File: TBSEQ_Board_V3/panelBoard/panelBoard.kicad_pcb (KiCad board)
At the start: 2 copper layers, 200 x 130.3 mm, 90 parts, among them J1 Conn_01x05, J14 Conn_01x05, U7 HT16K33_28SOP-A_

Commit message: V3Board
panelBoardアートワーク完了 ラベル未記入
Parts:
- removed J14: Conn_01x05, Connector_JST:JST_XH_B5B-XH-A_1x05_P2.50mm_Vertical
- removed VR1: RK09D117000B, SamacSys_Parts:RK09D117000B
- removed VR2, VR7, VR8: 50K(B), SamacSys_Parts:PTV1113420AA103
- removed VR3, VR5: 50K(A), SamacSys_Parts:PTV1113420AA103
- removed VR4: 50K(B)2連, SamacSys_Parts:PTV1124420AA504
- removed VR6: 1M(A), SamacSys_Parts:PTV1113420AA103
- removed VR9: 10K(A), SamacSys_Parts:PTV1113420AA103
- moved D13 141.9 mm to (138.3, 136.2)
- moved D14 141.9 mm to (149.2, 136.2)
- moved D15 141.9 mm to (159.9, 136.2)
- moved D16 141.9 mm to (170.2, 136.2)
- moved D19 141.9 mm to (182.5, 118.5)
- moved D21 141.9 mm to (186.0, 135.9)
- moved D32 141.9 mm to (145.4, 118.5)
- moved S12 141.9 mm to (160.4, 142.4)
- moved S13 141.9 mm to (171.0, 142.4)
- moved S19 141.9 mm to (222.6, 142.2)
- moved S20 141.9 mm to (222.0, 124.8)
- moved S21 141.9 mm to (207.8, 142.3)
- moved D10 141.9 mm to (106.4, 136.2)
- moved D11 141.9 mm to (117.1, 136.2)
- moved D12 141.9 mm to (127.6, 136.2)
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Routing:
- net COM2/KS1: track 0.00 -> 327.3 mm, vias 0 -> 1
- net COM0: track 0.00 -> 276.2 mm, vias 0 -> 1
- net COM1: track 0.00 -> 242.7 mm, vias 0 -> 3
- net RowK3: track 0.00 -> 223.5 mm, vias 0 -> 3
- net RowK11: track 0.00 -> 220.7 mm
- net Row8: track 0.00 -> 220.1 mm, vias 0 -> 1
- net COM1/KS0: track 0.00 -> 219.0 mm, vias 0 -> 2
- net Row0: track 0.00 -> 212.2 mm, vias 0 -> 2
- net Row4: track 0.00 -> 205.1 mm, vias 0 -> 1
- net RowK6: track 0.00 -> 203.8 mm
- net RowK4: track 0.00 -> 201.4 mm
- net Row11: track 0.00 -> 201.1 mm, vias 0 -> 2
- net RowK8: track 0.00 -> 197.0 mm
- net Row1: track 0.00 -> 193.9 mm, vias 0 -> 1
- net Row2: track 0.00 -> 193.3 mm, vias 0 -> 1
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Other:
- board size 200 x 130.3 mm -> 200 x 103 mm

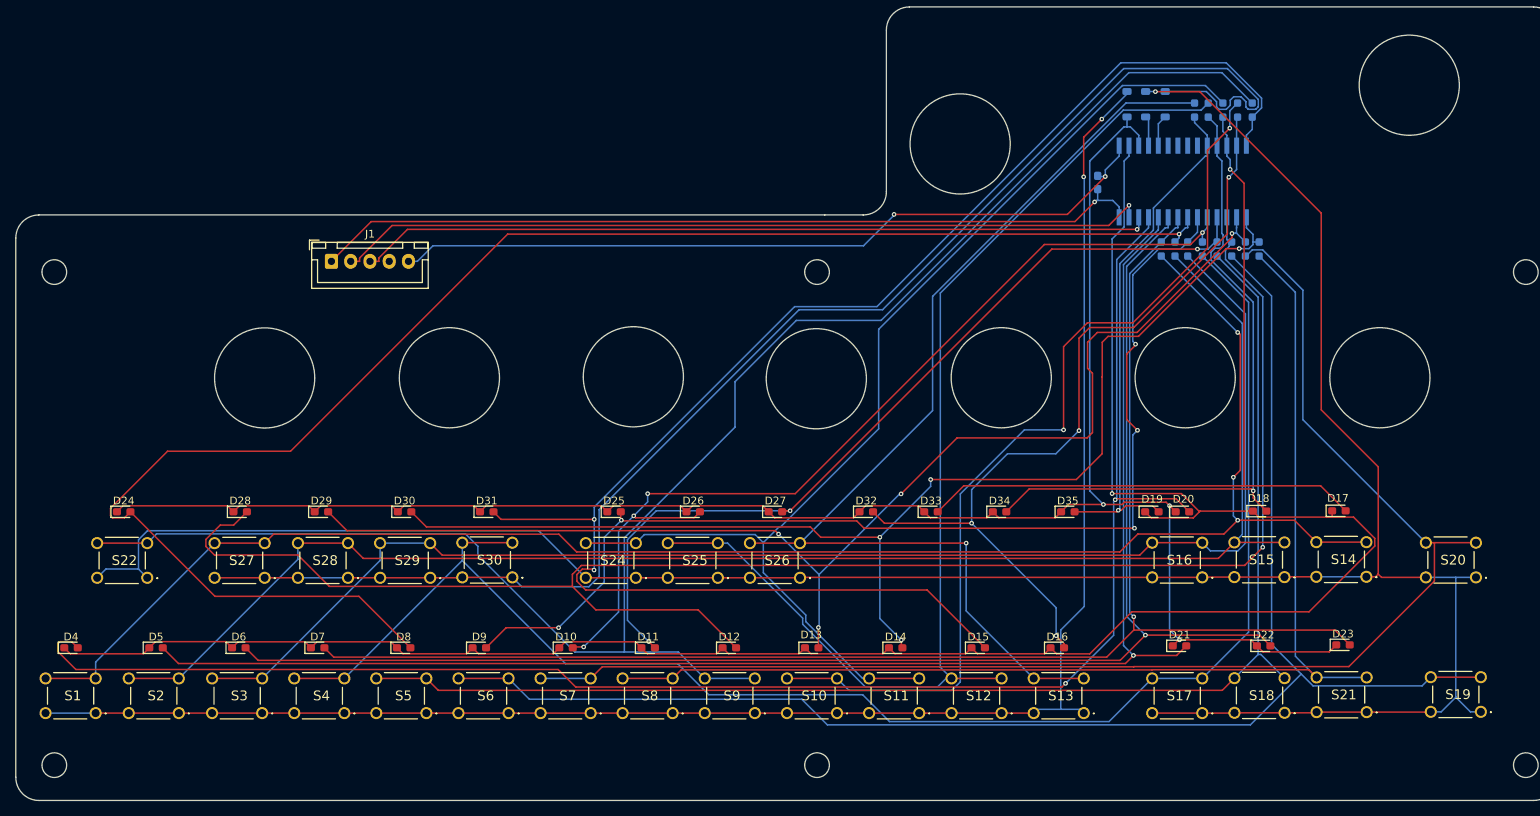
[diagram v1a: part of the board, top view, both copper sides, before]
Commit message: V3Board
PanelBoard⇒debugPanelBoardにして部品を全部表に出してアートワーク修正中
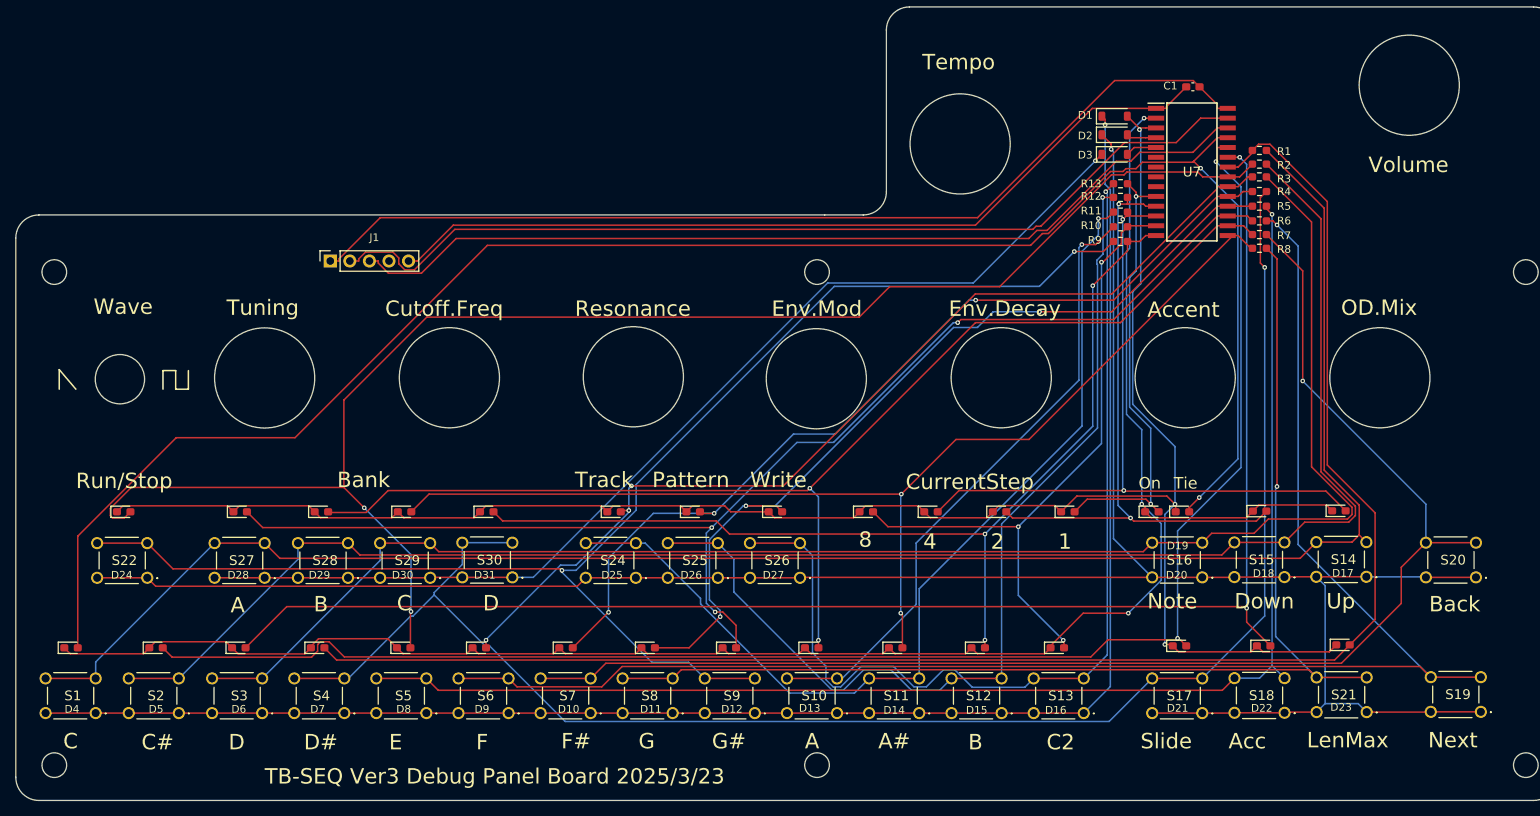
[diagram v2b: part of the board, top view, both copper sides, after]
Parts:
- C1, D1, D2, D3, R1, R10, R11, R12, R13, R2, R3, R4, R5, R6, R7, R8, R9, U7: moved to F.Cu
- J1: footprint Connector_JST:JST_XH_B5B-XH-A_1x05_P2.50mm_Vertical -> Connector_PinSocket_2.54mm:PinSocket_1x05_P2.54mm_Vertical
- moved R9 24.2 mm to (178.4, 83.4), turned to 180 degrees
- moved R10 21.5 mm to (178.4, 81.5), turned to 180 degrees
- moved R11 18.8 mm to (178.4, 79.6), turned to 180 degrees
- moved R1 18.1 mm to (196.4, 71.6), turned to 0 degrees
- moved C1 17.5 mm to (187.8, 63.4), turned to 180 degrees
- moved R12 16.1 mm to (178.4, 77.7), turned to 180 degrees
- moved R2 15.5 mm to (196.4, 73.4), turned to 0 degrees
- moved R13 13.6 mm to (178.4, 75.9), turned to 180 degrees
- moved R3 13.2 mm to (196.4, 75.1), turned to 0 degrees
- moved R4 10.5 mm to (196.4, 77.0), turned to 0 degrees
- moved D3 9.24 mm to (177.6, 72.1), turned to 0 degrees
- moved R5 7.82 mm to (196.4, 78.9), turned to 0 degrees
- moved D2 5.65 mm to (177.6, 69.6), turned to 0 degrees
- moved R6 5.12 mm to (196.4, 80.8), turned to 0 degrees
- moved R7 2.61 mm to (196.4, 82.5), turned to 0 degrees
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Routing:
- net Row11: track 201.1 -> 129.4 mm, vias 2 -> 3
- net Row8: track 220.1 -> 166.4 mm, vias 1 -> 3
- net COM3/KS2: track 187.3 -> 137.9 mm, vias 0 -> 1
- net RowK12: track 120.1 -> 81.4 mm, vias 2 -> 1
- net RowK11: track 220.7 -> 184.0 mm, vias 0 -> 2
- net COM0: track 276.2 -> 245.5 mm, vias 1 -> 3
- net COM2/KS1: track 327.3 -> 300.7 mm
- net Row0: track 212.2 -> 235.7 mm
- net RowK13: track 147.0 -> 124.2 mm, vias 0 -> 1
- net RowK5: track 185.3 -> 207.4 mm
- net Row12: track 108.6 -> 86.5 mm, vias 4 -> 3
- net RowK14: track 147.4 -> 125.9 mm, vias 0 -> 1
- net Row3: track 192.4 -> 213.5 mm, vias 1 -> 0
- net RowK4: track 201.4 -> 220.9 mm
- net D+3.3V: track 108.7 -> 128.1 mm, vias 1 -> 0
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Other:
- outline, holes or cut-outs redrawn
- board text added: "1"
- board text added: "2"
- board text added: "4"
- board text added: "8"
- board text added: "A"
- board text added: "A#"
- board text added: "Acc"
- board text added: "Accent"
- board text added: "B"
- board text added: "Back"
- board text added: "Bank"
- board text added: "C"
- board text added: "C#"
- board text added: "C2"
- board text added: "CurrentStep"
- board text added: "Cutoff.Freq"
- board text added: "D"
- board text added: "D#"
- board text added: "Down"
- board text added: "E"
- board text added: "Env.Decay"
- board text added: "Env.Mod"
- board text added: "F"
- board text added: "F#"
- board text added: "G"
- board text added: "G#"
- board text added: "LenMax"
- board text added: "Next"
- board text added: "Note"
- board text added: "OD.Mix"
- board text added: "On"
- board text added: "Pattern"
- board text added: "Resonance"
- board text added: "Run/Stop"
- board text added: "Slide"
- board text added: "TB-SEQ Ver3 Debug Panel Board 2025/3/23"
- board text added: "Tempo"
- board text added: "Tie"
- board text added: "Track"
- board text added: "Tuning"
- board text added: "Up"
- board text added: "Volume"
- board text added: "Wave"
- board text added: "Write"

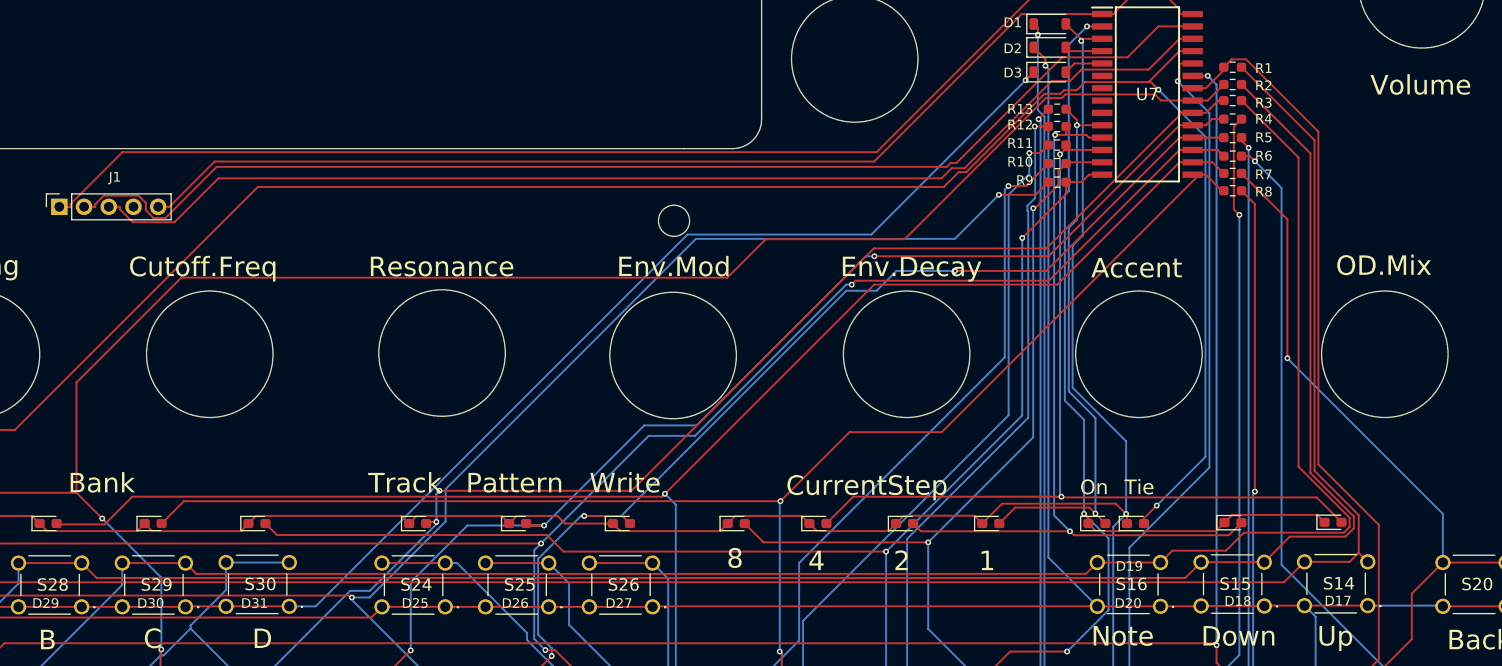
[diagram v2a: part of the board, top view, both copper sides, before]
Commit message: TBSEQ3
ハードウェアデバッグしたバージョン>mainBORAD_R1
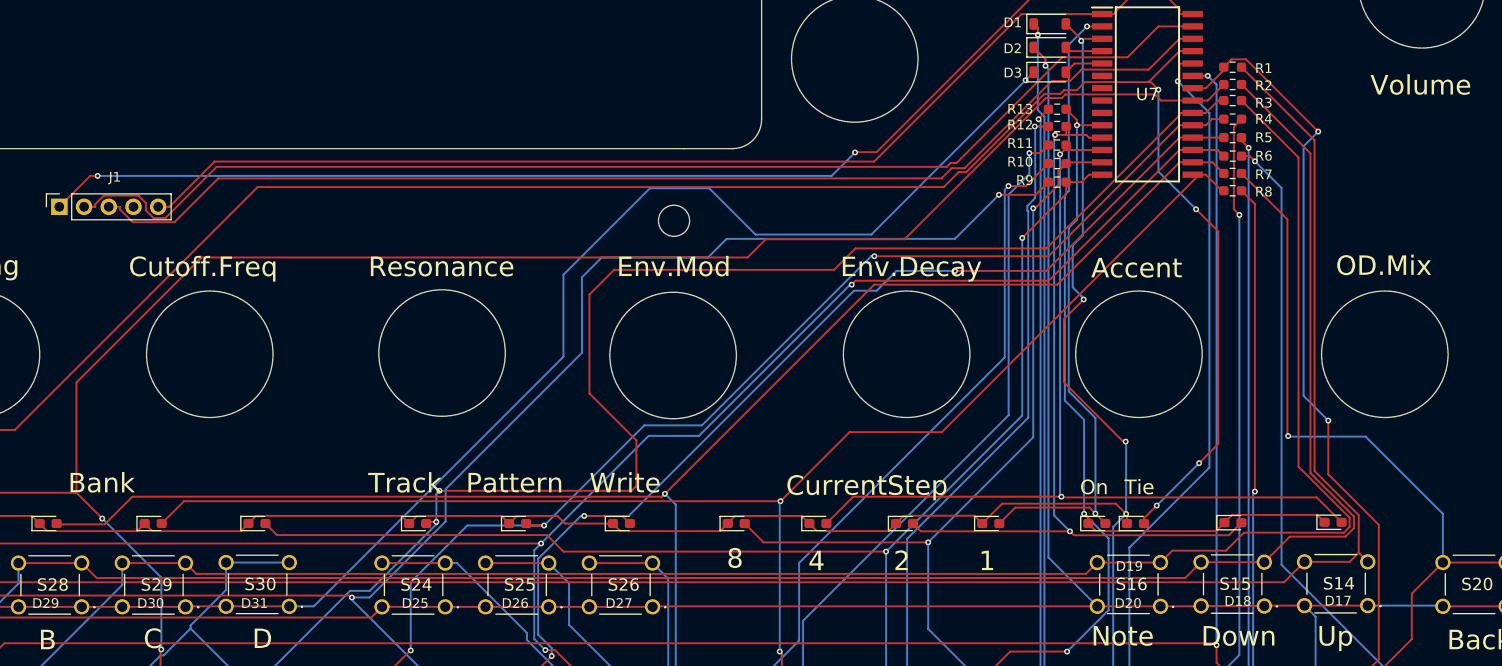
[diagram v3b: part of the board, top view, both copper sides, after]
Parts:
- D10, D11, D12, D13, D14, D15, D16, D17, D18, D19, D20, D21, D22, D23, D4, D5, D6, D7, D8, D9: value LED -> KT-0603R
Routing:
- net Row5: track 128.5 -> 146.9 mm
- net COM3/KS2: track 137.9 -> 146.8 mm
- net RowK9: track 180.0 -> 184.7 mm
- net RowK11: track 184.0 -> 188.5 mm
- net COM1: track 245.2 -> 247.0 mm, vias 3 -> 5
- net Row3: track 213.5 -> 214.7 mm, vias 0 -> 2
- net Row0: track 235.7 -> 236.8 mm, vias 2 -> 4
- net D+3.3V: track 128.1 -> 128.0 mm, vias 0 -> 2
